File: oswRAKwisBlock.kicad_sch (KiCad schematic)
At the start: 32 parts, among them J1 WisBlock, J2 0524352471, J3 USB_B_Micro, J4 10114830-10102LF, Q1 SI1308EDL-T1-GE3, U1 MCP73811T-420I/OT

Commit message: Adding a bunch of stuff to the design and some local models.
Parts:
- added AN1: 1.575GHz ANT, AllardANT:MOLEX_1462350001_CHIP, symbol AllardAnt:AN00000
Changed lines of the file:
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@@
+	)
+	(symbol
+		(lib_id "AllardAnt:AN00000")
+		(at 234.95 34.29 0)
+		(unit 1)
+		(exclude_from_sim no)
+		(in_bom yes)
+		(on_board yes)
+		(dnp no)
+		(fields_autoplaced yes)
+		(property "Reference" "AN1"
+			(at 240.03 26.0349 0)
+			(effects
+				(font
+					(size 1.524 1.524)
+				)
+				(justify left)
+			)
+		)
+		(property "Value" "1.575GHz ANT"
+			(at 240.03 28.5749 0)
+			(effects
+				(font
+					(size 1.524 1.524)
+				)
+				(justify left)
+			)
+		)
+		(property "Footprint" "AllardANT:MOLEX_1462350001_CHIP"
+			(at 237.998 54.61 0)
+			(effects
+				(font
+					(size 1.27 1.27)
+					(italic yes)
+				)
+				(hide yes)
+			)
+		)
+		(property "Datasheet" "https://www.molex.com/en-us/products/part-detail/1462350001?display=pdf"
+			(at 237.998 54.61 0)
+			(effects
+				(font
+					(size 1.27 1.27)
+					(italic yes)
+				)
+				(hide yes)
+			)
+		)
+		(property "Description" "1.575GHz antenna GPS"
+			(at 237.998 54.61 0)
+			(effects
+				(font
+					(size 1.27 1.27)
+				)
+				(hide yes)
+			)
+		)
+		(property "Manufacturer" "Molex"
+			(at 238.252 58.674 0)
+			(effects
+				(font
+					(size 1.27 1.27)
+				)
+				(hide yes)
+			)
+		)
+		(property "MPN" "1462350001"
+			(at 238.252 58.674 0)
+			(effects
+				(font
+					(size 1.27 1.27)
+				)
+				(hide yes)
+			)
+		)
+		(property "manf#" "1462350001"
+			(at 238.252 58.674 0)
+			(effects
+				(font
+					(size 1.27 1.27)
+				)
+				(hide yes)
+			)
+		)
+		(property "SUP1" "DigiKey"
+			(at 238.252 58.674 0)
+			(effects
+				(font
+					(size 1.27 1.27)
+				)
+				(hide yes)
+			)
+		)
+		(property "SUP1_PN" "WM15009CT-ND"
+			(at 238.252 58.674 0)
+			(effects
+				(font
+					(size 1.27 1.27)
+				)
+				(hide yes)
+			)
+		)
+		(property "SUP2" "Mouser"
+			(at 238.252 58.674 0)
+			(effects
+				(font
+					(size 1.27 1.27)
+				)
+				(hide yes)
+			)
+		)
+		(property "SUP2_PN" "538-146235-0001"
+			(at 238.252 58.674 0)
+			(effects
+				(font
+					(size 1.27 1.27)
+				)
+				(hide yes)
+			)
+		)
+		(property "SUP3" "LCSC"
+			(at 238.252 58.674 0)
+			(effects
+				(font
+					(size 1.27 1.27)
+				)
+				(hide yes)
+			)
+		)
+		(property "SUP3_PN" "C586446"
+			(at 238.252 58.674 0)
+			(effects
+				(font
+					(size 1.27 1.27)
+				)
+				(hide yes)
+			)
+		)
+		(property "variant" "default"
+			(at 238.252 58.674 0)
+			(effects
+				(font
+					(size 1.27 1.27)
+				)
+				(hide yes)
+			)
+		)
+		(property "Band" "1.561 GHz, 1.575 GHz, 1.602 GHz"
+			(at 237.998 54.61 0)
+			(effects
+				(font
+					(size 1.27 1.27)
+				)
+				(hide yes)
+			)
+		)
+		(property "Temperature" "-40-85"
+			(at 238.252 58.674 0)
+			(effects
+				(font
+					(size 1.27 1.27)
+				)
+				(hide yes)
+			)
+		)
+		(pin "4"
+		)
+		(pin "3"
+		)
+		(pin "1"
+		)
+		(pin "2"
+		)
+		(instances
+			(project "oswRAKwisBlock"
+				(path "/2fe076e6-bb0e-436f-836d-ec5f0ee79cef"
+					(reference "AN1")
+					(unit 1)
+				)
+			)
+		)
 	)
 	(symbol

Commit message: Working on the board a bit more.
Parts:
- removed J3: USB_B_Micro, AllardConnFootPrints:MOLEX_1051330011, symbol AllardConn:J10031
- added J5: USB micro, AllardConnFootPrints:GCT_USB3190-GF-C, symbol AllardConn:J10033
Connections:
- net GND: now also J5.5 (GND)
- net USB_+: now also J5.3 (D+)
- net USB_-: now also J5.2 (D-)
- net VUSB_BUS: now also J5.1 (VCC)
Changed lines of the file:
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@@
 	(wire
 		(pts
+			(xy 39.37 50.8) (xy 34.29 50.8)
+		)
+		(stroke
+			(width 0)
+			(type default)
+		)
+	)
+	(wire
+		(pts
 			(xy 194.31 67.31) (xy 199.39 67.31)
 		)
@@
 	(wire
 		(pts
-			(xy 31.75 50.8) (xy 34.29 50.8)
-		)
-		(stroke
-			(width 0)
-			(type default)
-		)
-	)
-	(wire
-		(pts
 			(xy 168.91 115.57) (xy 168.91 134.62)
 		)
@@
 	(wire
 		(pts
-			(xy 31.75 46.99) (xy 31.75 50.8)
-		)
-		(stroke
-			(width 0)
-			(type default)
-		)
-	)
-	(wire
-		(pts
 			(xy 177.8 105.41) (xy 199.39 105.41)
 		)
@@
 	(wire
 		(pts
+			(xy 39.37 44.45) (xy 39.37 50.8)
+		)
+		(stroke
+			(width 0)
+			(type default)
+		)
+	)
+	(wire
+		(pts
 			(xy 115.57 57.15) (xy 113.03 57.15)
 		)
@@
 	)
 	(label "USB_-"
-		(at 39.37 39.37 0)
+		(at 39.37 36.83 0)
 		(fields_autoplaced yes)
 		(effects
@@
 	)
 	(label "USB_+"
-		(at 39.37 36.83 0)
+		(at 39.37 34.29 0)
 		(fields_autoplaced yes)
 		(effects
@@
 	)
 	(symbol
+		(lib_id "AllardConn:J10033")
+		(at 26.67 40.64 0)
+		(unit 1)
+		(exclude_from_sim no)
+		(in_bom yes)
+		(on_board yes)
+		(dnp no)
+		(fields_autoplaced yes)
+		(property "Reference" "J5"
+			(at 29.845 24.13 0)
+			(effects
+				(font
+					(size 1.27 1.27)
+				)
+			)
+		)
+		(property "Value" "USB micro"
+			(at 29.845 26.67 0)
+			(effects
+				(font
+					(size 1.27 1.27)
+				)
+			)
+		)
+		(property "Footprint" "AllardConnFootPrints:GCT_USB3190-GF-C"
+			(at 29.21 61.976 0)
+			(effects
+				(font
+					(size 1.27 1.27)
+				)
+				(justify bottom)
+				(hide yes)
+			)
+		)
+		(property "Datasheet" "https://gct.co/files/specs/usb3190-spec.pdf"
+			(at 28.956 71.628 0)
+			(effects
+				(font
+					(size 1.27 1.27)
+				)
+				(hide yes)
+			)
+		)
+		(property "Description" "MICRO B SKT VERT MID MOUNT H=3.9"
+			(at 28.956 71.628 0)
+			(effects
+				(font
+					(size 1.27 1.27)
+				)
+				(hide yes)
+			)
+		)
+		(property "MPN" "USB3190-GF-C"
+			(at 28.956 71.628 0)
+			(effects
+				(font
+					(size 1.27 1.27)
+				)
+				(justify bottom)
+				(hide yes)
+			)
+		)
+		(property "manf#" "USB3190-GF-C"
+			(at 18.542 64.262 0)
+			(effects
+				(font
+					(size 1.27 1.27)
+				)
+				(justify bottom)
+				(hide yes)
+			)
+		)
+		(property "SUP1" "DigiKey"
+			(at 33.274 63.754 0)
+			(effects
+				(font
+					(size 1.27 1.27)
+				)
+				(justify bottom)
+				(hide yes)
+			)
+		)
+		(property "SUP1_PN" "2073-USB3190-GF-CCT-ND"
+			(at 26.924 62.992 0)
+			(effects
+				(font
+					(size 1.27 1.27)
+				)
+				(justify bottom)
+				(hide yes)
+			)
+		)
+		(property "SUP2" "Mouser"
+			(at 29.21 61.976 0)
+			(effects
+				(font
+					(size 1.27 1.27)
+				)
+				(justify bottom)
+				(hide yes)
+			)
+		)
+		(property "SUP2_PN" "640-USB3190-GF-C"
+			(at 29.21 61.976 0)
+			(effects
+				(font
+					(size 1.27 1.27)
+				)
+				(justify bottom)
+				(hide yes)
+			)
+		)
+		(property "SUP3" "LCSC"
+			(at 28.956 71.628 0)
+			(effects
+				(font
+					(size 1.27 1.27)
+				)
+				(justify bottom)
+				(hide yes)
+			)
+		)
+		(property "SUP3_PN" "C7407277"
+			(at 29.21 61.976 0)
+			(effects
+				(font
+					(size 1.27 1.27)
+				)
+				(justify bottom)
+				(hide yes)
+			)
+		)
+		(property "Temperature" "-30°C ~ 85°C"
+			(at 29.21 61.976 0)
+			(effects
+				(font
+					(size 1.27 1.27)
+				)
+				(justify bottom)
+				(hide yes)
+			)
+		)
+		(property "variant" "default"
+			(at 29.21 61.976 0)
+			(effects
+				(font
+					(size 1.27 1.27)
+				)
+				(justify bottom)
+				(hide yes)
+			)
+		)
+		(property "Manufacturer" "GCT"
+			(at 28.956 71.628 0)
+			(effects
+				(font
+					(size 1.27 1.27)
+				)
+				(justify bottom)
+				(hide yes)
+			)
+		)
+		(pin "5"
+		)
+		(pin "4"
+		)
+		(pin "S1"
+		)
+		(pin "S4"
+		)
+		(pin "3"
+		)
+		(pin "S2"
+		)
+		(pin "S3"
+		)
+		(pin "2"
+		)
+		(pin "1"
+		)
+		(instances
+			(project "oswRAKwisBlock"
+				(path "/2fe076e6-bb0e-436f-836d-ec5f0ee79cef"
+					(reference "J5")
+					(unit 1)
+				)
+			)
+		)
+	)
+	(symbol
 		(lib_id "AllardPassive:C10A72-10001")
 		(at 184.15 121.92 0)
@@
 					(unit 1)
 				)
-			)
-		)
-	)
-	(symbol
-		(lib_id "AllardConn:J10031")
-		(at 31.75 36.83 0)
-		(unit 1)
-		(exclude_from_sim no)
-		(in_bom yes)
-		(on_board yes)
-		(dnp no)
-		(fields_autoplaced yes)
-		(property "Reference" "J3"
-			(at 31.75 24.13 0)
-			(effects
-				(font
-					(size 1.27 1.27)
-				)
-			)
-		)
-		(property "Value" "USB_B_Micro"
-			(at 31.75 26.67 0)
-			(effects
-				(font
-					(size 1.27 1.27)
-				)
-			)
-		)
-		(property "Footprint" "AllardConnFootPrints:MOLEX_1051330011"
-			(at 35.052 65.786 0)
-			(effects
-				(font
-					(size 1.27 1.27)
-				)
-				(hide yes)
-			)
-		)
-		(property "Datasheet" "https://www.molex.com/en-us/products/part-detail/1051330011?display=pdf"
-			(at 35.306 62.738 0)
-			(effects
-				(font
-					(size 1.27 1.27)
-				)
-				(hide yes)
-			)
-		)
-		(property "Description" "CONN RCPT USB2.0 MICRO B SMD"
-			(at 33.782 68.834 0)
-			(effects
-				(font
-					(size 1.27 1.27)
-				)
-				(hide yes)
-			)
-		)
-		(property "manf#" "1051330011"
-			(at 33.02 26.67 0)
-			(effects
-				(font
-					(size 1.27 1.27)
-				)
-				(hide yes)
-			)
-		)
-		(property "MPN" "1051330011"
-			(at 31.75 36.83 0)
-			(effects
-				(font
-					(size 1.2446 1.2446)
-				)
-				(hide yes)
-			)
-		)
-		(property "Manufacturer" "GCT"
-			(at 31.75 36.83 0)
-			(effects
-				(font
-					(size 1.2446 1.2446)
-				)
-				(hide yes)
-			)
-		)
-		(property "SUP1" "Digi-Key"
-			(at 31.75 36.83 0)
-			(effects
-				(font
-					(size 1.2446 1.2446)
-				)
-				(hide yes)
-			)
-		)
-		(property "SUP1_PN" "WM10134CT-ND"
-			(at 6.604 69.342 0)
-			(effects
-				(font
-					(size 1.2446 1.2446)
-				)
-				(hide yes)
-			)
-		)
-		(property "SUP2" "Mouser"
-			(at 31.75 36.83 0)
-			(effects
-				(font
-					(size 1.2446 1.2446)
-				)
-				(hide yes)
-			)
-		)
-		(property "SUP2_PN" "538-105133-0011"
-			(at 65.532 68.834 0)
-			(effects
-				(font
-					(size 1.2446 1.2446)
-				)
-				(hide yes)
-			)
-		)
-		(property "AI_PN" "${SYMBOL_NAME}"
-			(at 31.75 36.83 0)
-			(effects
-				(font
-					(size 1.2446 1.2446)
-				)
-				(hide yes)
-			)
-		)
-		(property "variant" "default"
-			(at 31.75 36.83 0)
-			(effects
-				(font
-					(size 1.27 1.27)
-				)
-				(hide yes)
-			)
-		)
-		(property "SUP3" "LCSC"
-			(at 31.75 36.83 0)
-			(effects
-				(font
-					(size 1.2446 1.2446)
-				)
-				(hide yes)
-			)
-		)
-		(property "SUP3_PN" " C586226"
-			(at 31.75 36.83 0)
-			(effects
-				(font
-					(size 1.2446 1.2446)
-				)
-				(hide yes)
-			)
-		)
-		(pin "4"
-		)
-		(pin "1"
-		)
-		(pin "3"
-		)
-		(pin "5"
-		)
-		(pin "6"
-		)
-		(pin "2"
-		)
-		(instances
-			(project "oswRAKwisBlock"
-				(path "/2fe076e6-bb0e-436f-836d-ec5f0ee79cef"
-					(reference "J3")
-					(unit 1)
-				)

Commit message: Working on things.
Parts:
- added C12, C13: 1u, AllardChip:CAPC100X50X60L25L, symbol AllardPassive:C10A72-10000
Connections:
- net GND: now also J1.3 (GND), J1.4 (GND), C12.2, C13.2
- net VDD: now also J1.6 (3V3), C12.1, C13.1
- net BTN1: now reaches R1.2, S1.1, S1.3 (K)
- net ~{MCU_RES}: now reaches J1.13 (RESET), R3.2
- net BTN2: now reaches R2.2, S2.1, S2.3 (K)
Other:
- moved on the sheet: C1, C10, C11, C2, C3, C4, C5, C6, C7, C8, C9, D1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

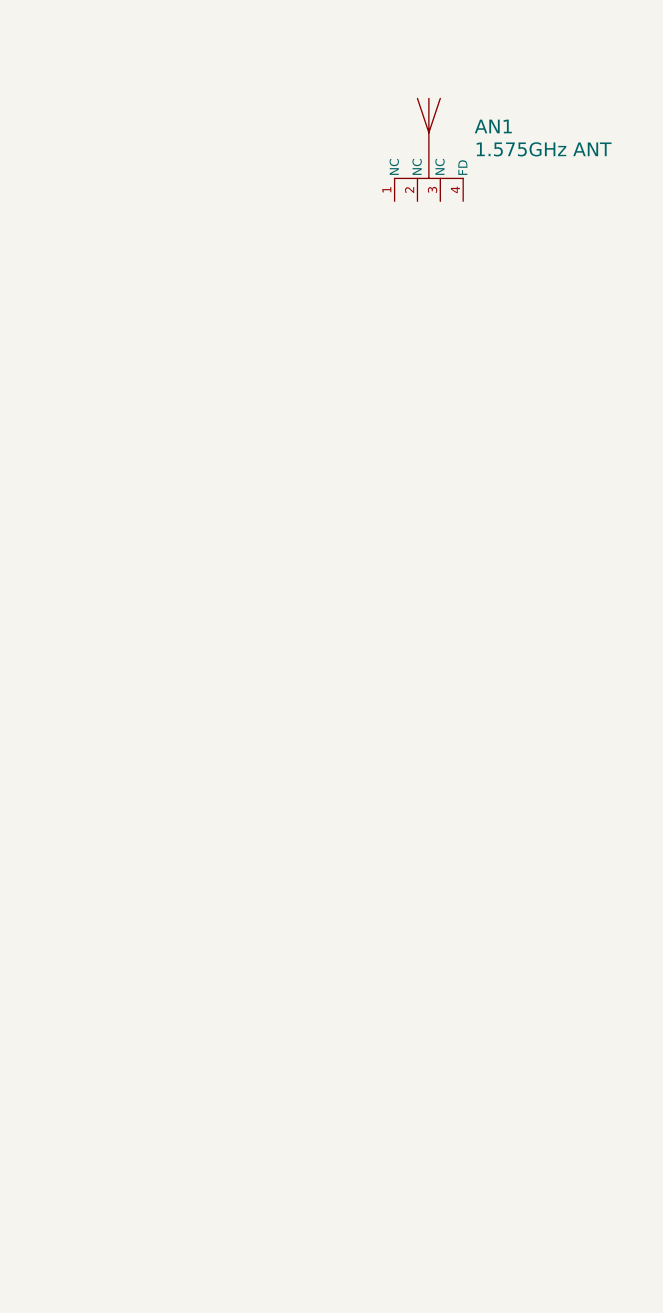
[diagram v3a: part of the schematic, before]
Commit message: Finally got the GPS chip wired in.  Just need to finish the pinout and then finalize the GPS part placement.
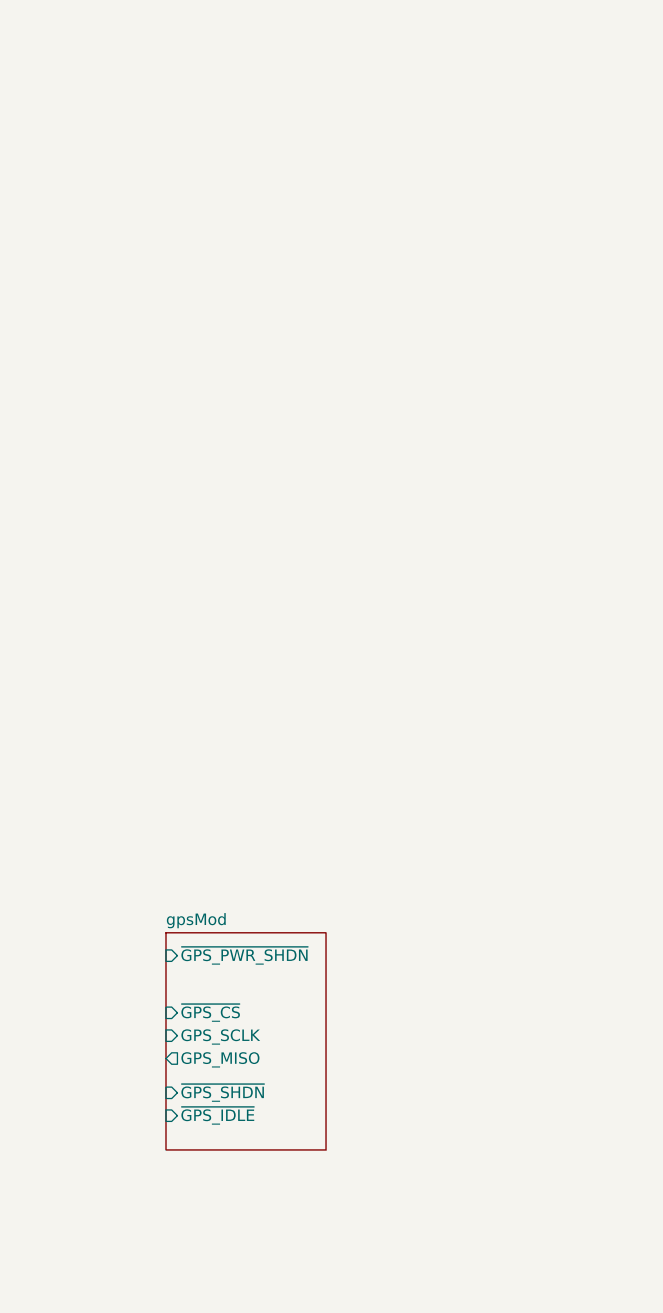
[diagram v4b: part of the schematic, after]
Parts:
- removed AN1: 1.575GHz ANT, AllardANT:MOLEX_1462350001_CHIP, symbol AllardAnt:AN00000
- D1, D2, D3: footprint AllardSOD:SOD370X155X135L32X57N -> AllardSOD:SOD370X155X135L32X57L
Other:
- added sheet gpsMod (gpsMod.kicad_sch)
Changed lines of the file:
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@@
 			)
 		)
-		(property "Footprint" "AllardSOD:SOD370X155X135L32X57N"
+		(property "Footprint" "AllardSOD:SOD370X155X135L32X57L"
 			(at 107.315 99.695 0)
 			(effects
@@
 	)
 	(symbol
-		(lib_id "AllardAnt:AN00000")
-		(at 234.95 34.29 0)
-		(unit 1)
-		(exclude_from_sim no)
-		(in_bom yes)
-		(on_board yes)
-		(dnp no)
-		(fields_autoplaced yes)
-		(property "Reference" "AN1"
-			(at 240.03 26.0349 0)
-			(effects
-				(font
-					(size 1.524 1.524)
-				)
-				(justify left)
-			)
-		)
-		(property "Value" "1.575GHz ANT"
-			(at 240.03 28.5749 0)
-			(effects
-				(font
-					(size 1.524 1.524)
-				)
-				(justify left)
-			)
-		)
-		(property "Footprint" "AllardANT:MOLEX_1462350001_CHIP"
-			(at 237.998 54.61 0)
-			(effects
-				(font
-					(size 1.27 1.27)
-					(italic yes)
-				)
-				(hide yes)
-			)
-		)
-		(property "Datasheet" "https://www.molex.com/en-us/products/part-detail/1462350001?display=pdf"
-			(at 237.998 54.61 0)
-			(effects
-				(font
-					(size 1.27 1.27)
-					(italic yes)
-				)
-				(hide yes)
-			)
-		)
-		(property "Description" "1.575GHz antenna GPS"
-			(at 237.998 54.61 0)
-			(effects
-				(font
-					(size 1.27 1.27)
-				)
-				(hide yes)
-			)
-		)
-		(property "Manufacturer" "Molex"
-			(at 238.252 58.674 0)
-			(effects
-				(font
-					(size 1.27 1.27)
-				)
-				(hide yes)
-			)
-		)
-		(property "MPN" "1462350001"
-			(at 238.252 58.674 0)
-			(effects
-				(font
-					(size 1.27 1.27)
-				)
-				(hide yes)
-			)
-		)
-		(property "manf#" "1462350001"
-			(at 238.252 58.674 0)
-			(effects
-				(font
-					(size 1.27 1.27)
-				)
-				(hide yes)
-			)
-		)
-		(property "SUP1" "DigiKey"
-			(at 238.252 58.674 0)
-			(effects
-				(font
-					(size 1.27 1.27)
-				)
-				(hide yes)
-			)
-		)
-		(property "SUP1_PN" "WM15009CT-ND"
-			(at 238.252 58.674 0)
-			(effects
-				(font
-					(size 1.27 1.27)
-				)
-				(hide yes)
-			)
-		)
-		(property "SUP2" "Mouser"
-			(at 238.252 58.674 0)
-			(effects
-				(font
-					(size 1.27 1.27)
-				)
-				(hide yes)
-			)
-		)
-		(property "SUP2_PN" "538-146235-0001"
-			(at 238.252 58.674 0)
-			(effects
-				(font
-					(size 1.27 1.27)
-				)
-				(hide yes)
-			)
-		)
-		(property "SUP3" "LCSC"
-			(at 238.252 58.674 0)
-			(effects
-				(font
-					(size 1.27 1.27)
-				)
-				(hide yes)
-			)
-		)
-		(property "SUP3_PN" "C586446"
-			(at 238.252 58.674 0)
-			(effects
-				(font
-					(size 1.27 1.27)
-				)
-				(hide yes)
-			)
-		)
-		(property "variant" "default"
-			(at 238.252 58.674 0)
-			(effects
-				(font
-					(size 1.27 1.27)
-				)
-				(hide yes)
-			)
-		)
-		(property "Band" "1.561 GHz, 1.575 GHz, 1.602 GHz"
-			(at 237.998 54.61 0)
-			(effects
-				(font
-					(size 1.27 1.27)
-				)
-				(hide yes)
-			)
-		)
-		(property "Temperature" "-40-85"
-			(at 238.252 58.674 0)
-			(effects
-				(font
-					(size 1.27 1.27)
-				)
-				(hide yes)
-			)
-		)
-		(pin "4"
-		)
-		(pin "3"
-		)
-		(pin "1"
-		)
-		(pin "2"
-		)
-		(instances
-			(project "oswRAKwisBlock"
-				(path "/2fe076e6-bb0e-436f-836d-ec5f0ee79cef"
-					(reference "AN1")
-					(unit 1)
-				)
-			)
-		)
-	)
-	(symbol
 		(lib_id "power:GND")
 		(at 40.64 129.54 0)
@@
 			)
 		)
-		(property "Footprint" "AllardSOD:SOD370X155X135L32X57N"
+		(property "Footprint" "AllardSOD:SOD370X155X135L32X57L"
 			(at 117.475 76.835 0)
 			(effects
@@
 			)
 		)
-		(property "Footprint" "AllardSOD:SOD370X155X135L32X57N"
+		(property "Footprint" "AllardSOD:SOD370X155X135L32X57L"
 			(at 117.475 89.535 0)
 			(effects
@@
 				)
 			)
+		)
+	)
+	(sheet
+		(at 205.74 115.57)
+		(size 17.78 24.13)
+		(fields_autoplaced yes)
+		(stroke
+			(width 0.1524)
+			(type solid)
+		)
+		(fill
+			(color 0 0 0 0.0000)
+		)
+		(property "Sheetname" "gpsMod"
+			(at 205.74 114.8584 0)
+			(effects
+				(font
+					(size 1.27 1.27)
+				)
+				(justify left bottom)
+			)
+		)
+		(property "Sheetfile" "gpsMod.kicad_sch"
+			(at 205.74 140.2846 0)
+			(effects
+				(font
+					(size 1.27 1.27)
+				)
+				(justify left top)
+				(hide yes)
+			)
+		)
+		(pin "~{GPS_PWR_SHDN}" input
+			(at 205.74 118.11 180)
+			(effects
+				(font
+					(size 1.27 1.27)
+				)
+				(justify left)
+			)
+		)
+		(pin "GPS_SCLK" input
+			(at 205.74 127 180)
+			(effects
+				(font
+					(size 1.27 1.27)
+				)
+				(justify left)
+			)
+		)
+		(pin "GPS_MISO" output
+			(at 205.74 129.54 180)
+			(effects
+				(font
+					(size 1.27 1.27)
+				)
+				(justify left)
+			)
+		)
+		(pin "~{GPS_CS}" input
+			(at 205.74 124.46 180)
+			(effects
+				(font
+					(size 1.27 1.27)
+				)
+				(justify left)
+			)
+		)
+		(pin "~{GPS_SHDN}" input
+			(at 205.74 133.35 180)
+			(effects
+				(font
+					(size 1.27 1.27)
+				)
+				(justify left)
+			)
+		)
+		(pin "~{GPS_IDLE}" input
+			(at 205.74 135.89 180)
+			(effects
+				(font
+					(size 1.27 1.27)
+				)
+				(justify left)
+			)
+		)
+		(instances
+			(project "oswRAKwisBlock"
+				(path "/2fe076e6-bb0e-436f-836d-ec5f0ee79cef"
+					(page "2")
+				)
+			)

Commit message: starting to lay the board out.
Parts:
- added C16: 1uF, AllardChip:CAPC60X30X39L17L, symbol AllardPassive:C10A71-10000
- added R8, R9: 10k, AllardChip:RESC40X20X15L10L, symbol AllardPassive:R10020-10000
- added U5: MIC5365-3.0YC5-TR, AllardSOT:SOT23-5P65_210X110L33X22L, symbol AllardPower:U40001
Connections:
- net BTN1: now also J1.30 (IO2)
- net BTN2: now also J1.32 (IO4)
- net BUSY: now also J1.29 (IO1)
- net GND: now also J1.FS3 (GND), C16.2, U5.2 (GND)
- net MOSI: now also J1.28 (SPI_MOSI)
- net RES: now also J1.31 (IO3)
- net SCLK: now also J1.26 (SPI_CLK)
- net SS: now also J1.25 (SPI_CS)
- net VDD: now also C16.1, R8.1, R9.1, U5.5 (VOUT)
- net ~{GPS_PWR_SHDN}: now reaches J1.22 (AIN1)
- net ~{GPS_PWR_SHDN}: now also R9.2
- net at J1.23 (BOOT): now also R8.2
- net ~{GPS_SHDN}: now reaches J1.24 (IO7)
- net GPS_MISO: now reaches J1.27 (SPI_MISO)
- net ~{GPS_IDLE}: now reaches J1.37 (IO5)
- net ~{GPS_CS}: now reaches J1.38 (IO6)
- net at C11.1, J4.1, U1.3 (V_{BAT}): now also U5.1 (VIN)
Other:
- moved on the sheet: C1, C12, C13, C2, C3, C4, C5, C6, C7, C8, C9, D1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
